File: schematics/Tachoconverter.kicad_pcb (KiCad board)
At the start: 2 copper layers, 46 x 68 mm, 30 parts, among them J1 Motor, J2 HC05, J3 Input, J4 Conn_01x01, J5 Conn_01x02, J6 Conn_01x07, J7 Conn_01x01, J8 Conn_01x07, J9 Conn_01x01, U1 AT24CS64-SSHM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

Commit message: board changed
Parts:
- removed U3: 74LVC2GU04, Package_TO_SOT_SMD:SOT-23-6_Handsoldering
- added J10: Conn_01x05, Connector_PinHeader_2.54mm:PinHeader_1x05_P2.54mm_Vertical, F.Cu at (163.7, 120.5)
- added R5: 1k, Resistor_SMD:R_1206_3216Metric_Pad1.30x1.75mm_HandSolder, B.Cu at (152.7, 77.4)
- added R6: 1k, Resistor_SMD:R_1206_3216Metric_Pad1.30x1.75mm_HandSolder, B.Cu at (150.4, 77.4)
- added U5: 74HC14, Package_SO:SOIC-14_3.9x8.7mm_P1.27mm, B.Cu at (152.7, 100.2)
- J8: value Conn_01x07 -> Conn_01x01; footprint Connector_PinHeader_2.54mm:PinHeader_1x07_P2.54mm_Vertical -> Connector_PinHeader_2.54mm:PinHeader_1x01_P2.54mm_Vertical
- moved R4 29.3 mm to (153.9, 106.2), turned to 180 degrees
- moved J8 15.2 mm to (164.0, 102.7)
- moved D2 10.8 mm to (154.8, 110.7)
- moved R3 10.4 mm to (152.1, 116.0), turned to 0 degrees
- moved J9 2.93 mm to (148.7, 92.5)
- moved JP1 2.10 mm to (146.1, 134.1)
- moved U2 0.64 mm to (168.0, 124.7)
- moved J6 0.38 mm to (148.0, 107.8)
- moved J4 0.28 mm to (148.7, 87.8)
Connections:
- A1 pad 22: /VSpeedIn -> Net-(A1-D0/SDA2)
- A1 pad 27: Net-(A1-D5/MISO1) -> /VSpeedIn
- A1 pad 32: Net-(A1-D10) -> /~{HC05ON}
- A1 pad 33: unconnected-(A1-D11-Pad33) -> Net-(A1-D11)
- J1 pad 2: /MotorSpeed -> Net-(J1-Pin_2)
- J2 pad 5: +5V -> Net-(J2-Pin_5)
- J7 pad 1: Net-(A1-D10) -> Net-(A1-D11)
- J8 pad 1: Net-(A1-D1/SCL2) -> Net-(A1-D7/SS1)
- R4 pad 1: +3V3 -> +5V
- R4 pad 2: /MotorSpeed -> Net-(J1-Pin_2)
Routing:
- net GND: track 288.7 -> 407.1 mm
- net Net-(J2-Pin_5): track 0.00 -> 50.0 mm
- net /MotorSpeed: track 48.5 -> 14.1 mm
- net /VSpeedIn: track 46.1 -> 24.6 mm, vias 0 -> 2
- net Net-(J1-Pin_2): track 0.00 -> 21.4 mm
- net /~{HC05ON}: track 0.00 -> 19.0 mm
- net +5V: track 105.8 -> 91.6 mm
- net /MotorPWM: track 32.2 -> 41.1 mm
- net /SDA: track 22.0 -> 30.1 mm
- net Net-(J1-Pin_5): track 22.3 -> 28.8 mm
- net Net-(D2-K-Pad3): track 8.85 -> 15.2 mm
- net /EN: track 26.0 -> 31.7 mm
- net /SCL: track 22.1 -> 26.9 mm
- net Net-(A1-D11): track 0.00 -> 4.45 mm
- net VCC: track 76.0 -> 72.3 mm
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
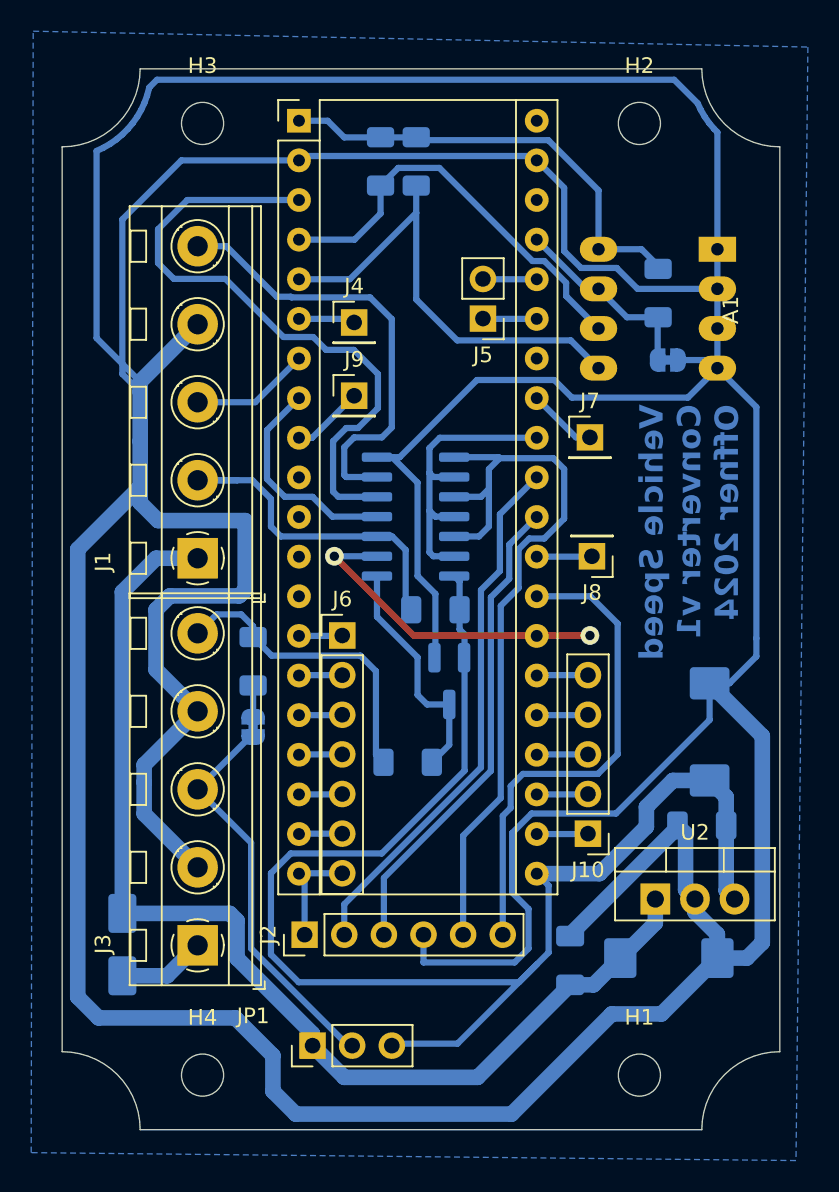
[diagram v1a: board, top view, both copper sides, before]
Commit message: schematic update
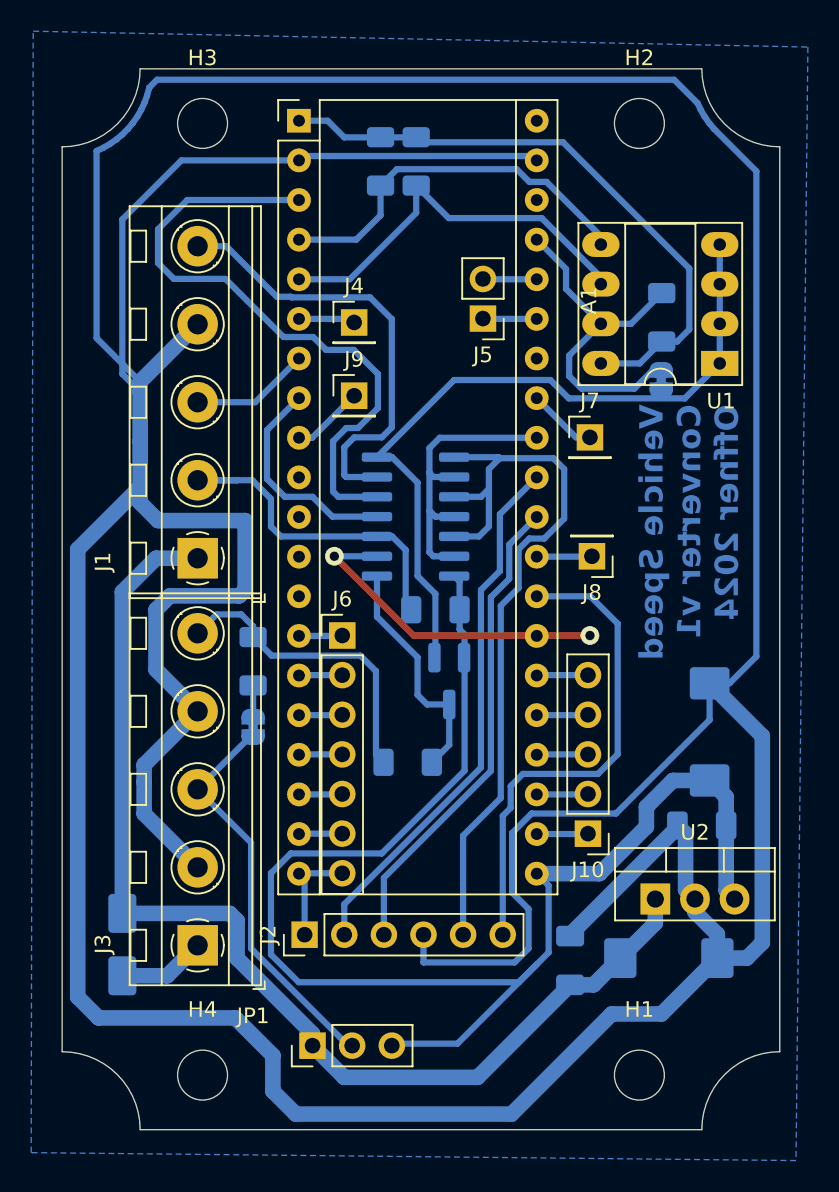
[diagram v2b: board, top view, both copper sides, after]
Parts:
- H1, H2, H3, H4: footprint MountingHole:MountingHole_2.7mm_M2.5 -> MountingHole:MountingHole_3.2mm_M3
- U1: moved to F.Cu
- moved U1 7.32 mm to (172.2, 90.4)
- moved R2 1.57 mm to (168.4, 87.4), turned to 90 degrees
- moved JP3 1.35 mm to (168.4, 91.5), turned to 90 degrees
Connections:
- A1 pad 4: /SCL -> /SDA
- A1 pad 5: /SDA -> /SCL
- R5 pad 2: /SDA -> /SCL
- R6 pad 2: /SCL -> /SDA
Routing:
- net GND: track 407.1 -> 395.9 mm
- net /WP: track 11.7 -> 22.7 mm
- net +3V3: track 29.0 -> 39.4 mm
- net /SDA: track 30.1 -> 24.6 mm
- net /SCL: track 26.9 -> 25.7 mm
